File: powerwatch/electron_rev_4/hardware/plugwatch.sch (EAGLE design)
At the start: 127 parts, among them J1 CON_MICRO_SDDM3AT-SF-PEJM5, U1 BGA725L6-ALT, U10 SIP32510, U12 SIP32510, U13 AB1815-T3, U16 MAX6746, U2 SAFFB1G56KB0F0A, U20 DS2401P+, U3 IRM-03-5V, U4 MAX-M8, U5 OPA369, U6 LIS2DW12, U8 OPA369, U9 SIP32510, X1 ABS07-32.768KHZ-7-T

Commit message: renumbered eagle parts
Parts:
- removed C19: 0.1uF, passives:CAPACITOR0402_CAP
- removed C26: 4.7uF, passives:CAPACITOR0402_CAP
- removed D11: (no value), passives:DIODE_SCHOTTKYSOD323
- removed J4: (no value), SparkFun-Connectors:JST_2MM_MALE
- removed RF, RF1: 4.99k 1%, passives:RESISTOR0402_RES
- removed RI1, RI3: 953k 1%, passives:RESISTOR1206_RES_HIGH_CLEARANCE
- removed RI2, RI4: 953k 1%, passives:RESISTOR0402_RES
- removed U16: MAX6746, chips:MAX6746
- removed U20: DS2401P+, DS2401P+:DS2401P+
- added C10: 1uF, passives:CAPACITOR0402_CAP
- added C16: 100uF, passives:CAPACITOR1210_CAP
- added D2: (no value), passives:DIODE_SCHOTTKYSOD323
- added J2: (no value), SparkFun-Connectors:JST_2MM_MALE
- added R20: 34k, passives:RESISTOR0402_RES
- added R37, R38, R39, R40: 1M, passives:RESISTOR0402_RES
- added U11: SIP32510, chips:SIP32510
- added U14: (no value), microphones:SPH0645LM4H-B
- added V1: S14K385, varistor:S14K385
- C1: value 1uF -> 47pF
- C11: value 10nF -> 1uF
- C12: value 10nF -> 4.7uF; DESCRIPTION CAP CER 10000PF 50V X7R 0402 -> CAP CER 4.7UF 6.3V X5R 0402; DIGIKEY 490-7763-1-ND -> 445-5947-1-ND; MANUFACTURER Murata -> TDK; MPN GRM155R71H103JA88D -> C1005X5R0J475K050BC
- C15: value 100nF -> 100uF; device passives:CAPACITOR0402_CAP -> passives:CAPACITOR1210_CAP; DESCRIPTION CAP CER 0.1UF 10V X7R 0402 -> (none); DIGIKEY 490-10777-1-ND -> (none); MANUFACTURER Murata -> (none); MPN GRM155R71A104JA01D -> (none)
- C17: value 100uF -> 2000uF; device passives:CAPACITOR1210_CAP -> rcl:CPOL-USE5-13
- C2: value 2000uF -> 10nF; device rcl:CPOL-USE5-13 -> passives:CAPACITOR0402_CAP; DESCRIPTION (none) -> CAP CER 10000PF 50V X7R 0402; DIGIKEY (none) -> 490-7763-1-ND; MANUFACTURER (none) -> Murata; MPN (none) -> GRM155R71H103JA88D
- C3: value 47pF -> 10nF; DESCRIPTION (none) -> CAP CER 10000PF 50V X7R 0402; DIGIKEY (none) -> 490-7763-1-ND; MANUFACTURER (none) -> Murata; MPN (none) -> GRM155R71H103JA88D
- C4: value 1uF -> 0.1uF; DESCRIPTION CAP CER 10000PF 50V X7R 0402 -> CAP CER 0.1UF 10V X7R 0402; DIGIKEY 490-7763-1-ND -> 490-10777-1-ND; MPN GRM155R71H103JA88D -> GRM155R71A104JA01D
- C7: value 100uF -> 100nF; device passives:CAPACITOR1210_CAP -> passives:CAPACITOR0402_CAP; DESCRIPTION (none) -> CAP CER 0.1UF 10V X7R 0402; DIGIKEY (none) -> 490-10777-1-ND; MANUFACTURER (none) -> Murata; MPN (none) -> GRM155R71A104JA01D
- D1: value BLUE -> (none); device leds:LED0603 -> passives:DIODE_SCHOTTKYSOD323; DIGIKEY 160-1837-6-ND -> CUS10S30H3FCT-ND; MANUFACTURER (none) -> toshiba; MPN (none) -> CUS10S30,H3F
- D4: value 3.3V -> (none); device passives:DIODE_ZENERSOT323 -> passives:DIODE_SCHOTTKYSOD323; DIGIKEY MM3Z3V3BCT-ND -> CUS10S30H3FCT-ND; MANUFACTURER ON Semiconductor -> toshiba; MPN MM3Z3V3B -> CUS10S30,H3F
- D5, D6, D7: value 3.3V -> (none)
- D8: device passives:DIODE_SCHOTTKYSOD323 -> passives:DIODE_ZENERSOT323; DIGIKEY CUS10S30H3FCT-ND -> MM3Z3V3BCT-ND; MANUFACTURER toshiba -> ON Semiconductor; MPN CUS10S30,H3F -> MM3Z3V3B
- D9: value (none) -> BLUE; device passives:DIODE_SCHOTTKYSOD323 -> leds:LED0603; DIGIKEY CUS10S30H3FCT-ND -> 160-1837-6-ND; MANUFACTURER toshiba -> (none); MPN CUS10S30,H3F -> (none)
- R1: value 10k -> 66.5; DESCRIPTION RES SMD 150 OHM 1% 1/16W 0402 -> RES SMD 1K OHM 1% 1/16W 0402; DIGIKEY RMCF0402FT150RCT-ND -> RMCF0402FT1K00CT-ND; MPN RMCF0402FT150R -> RMCF0402FT1K00
- R10: value 10k -> 5k; DESCRIPTION RES SMD 10K OHM 1% 1/16W 0402 -> RES SMD 150 OHM 1% 1/16W 0402; DIGIKEY RMCF0402FT10K0CT-ND -> RMCF0402FT150RCT-ND; MPN RMCF0402FT10K0 -> RMCF0402FT150R
- R11: value 68 -> 10k
- R15: value 100k -> 10k; DESCRIPTION RES SMD 150 OHM 1% 1/16W 0402 -> RES SMD 10K OHM 1% 1/16W 0402; DIGIKEY RMCF0402FT150RCT-ND -> RMCF0402FT10K0CT-ND; MPN RMCF0402FT150R -> RMCF0402FT10K0
- R16, R17, R18, R19: value 100k -> 10k; DESCRIPTION RES SMD 100K OHM 1% 1/16W 0402 -> RES SMD 150 OHM 1% 1/16W 0402; DIGIKEY 1276-3432-1-ND -> RMCF0402FT150RCT-ND; MANUFACTURER Samsung -> Stackpole Electronics; MPN RC1005F104CS -> RMCF0402FT150R
- R2: value 10k -> 68; DESCRIPTION RES SMD 150 OHM 1% 1/16W 0402 -> RES SMD 10K OHM 1% 1/16W 0402; DIGIKEY RMCF0402FT150RCT-ND -> RMCF0402FT10K0CT-ND; MPN RMCF0402FT150R -> RMCF0402FT10K0
- R21: value 750k -> 100k; device passives:RESISTOR1206_RES_HIGH_CLEARANCE -> passives:RESISTOR0402_RES; DESCRIPTION RES SMD 150 OHM 1% 1/16W 0402 -> RES SMD 100K OHM 1% 1/16W 0402; DIGIKEY RMCF0402FT150RCT-ND -> 1276-3432-1-ND; MANUFACTURER Stackpole Electronics -> Samsung; MPN RMCF0402FT150R -> RC1005F104CS
- R22, R23: value 1M 1% -> 100k; DESCRIPTION (none) -> RES SMD 100K OHM 1% 1/16W 0402; DIGIKEY P1.00MLCT-ND -> 1276-3432-1-ND; MANUFACTURER (none) -> Samsung; MPN (none) -> RC1005F104CS
- R24: value 835k -> 100k; DESCRIPTION RES SMD 150 OHM 1% 1/16W 0402 -> RES SMD 100K OHM 1% 1/16W 0402; DIGIKEY RMCF0402FT150RCT-ND -> 1276-3432-1-ND; MANUFACTURER Stackpole Electronics -> Samsung; MPN RMCF0402FT150R -> RC1005F104CS
- R25: value 1M 1% -> 100k; DESCRIPTION (none) -> RES SMD 150 OHM 1% 1/16W 0402; DIGIKEY P1.00MLCT-ND -> RMCF0402FT150RCT-ND; MANUFACTURER (none) -> Stackpole Electronics; MPN (none) -> RMCF0402FT150R
- R26: value 68 -> 100k; DESCRIPTION RES SMD 10K OHM 1% 1/16W 0402 -> RES SMD 150 OHM 1% 1/16W 0402; DIGIKEY RMCF0402FT10K0CT-ND -> RMCF0402FT150RCT-ND; MPN RMCF0402FT10K0 -> RMCF0402FT150R
- R28: value 1M 1% -> 750k; device passives:RESISTOR0402_RES -> passives:RESISTOR1206_RES_HIGH_CLEARANCE; DESCRIPTION (none) -> RES SMD 150 OHM 1% 1/16W 0402; DIGIKEY P1.00MLCT-ND -> RMCF0402FT150RCT-ND; MANUFACTURER (none) -> Stackpole Electronics; MPN (none) -> RMCF0402FT150R
- R29: value 5K -> 750k; device passives:RESISTOR0402_RES -> passives:RESISTOR1206_RES_HIGH_CLEARANCE
- R32: value 1.5k -> 835k
- R33: value 1.5k -> 953k; DESCRIPTION RES SMD 150 OHM 1% 1/16W 0402 -> (none); DIGIKEY RMCF0402FT150RCT-ND -> P953KLCT-ND; MANUFACTURER Stackpole Electronics -> (none); MPN RMCF0402FT150R -> (none)
- R34: value 10k -> 953k; DESCRIPTION RES SMD 150 OHM 1% 1/16W 0402 -> (none); DIGIKEY RMCF0402FT150RCT-ND -> P953KLCT-ND; MANUFACTURER Stackpole Electronics -> (none); MPN RMCF0402FT150R -> (none)
- R35: value 66.5 -> 953k; device passives:RESISTOR0402_RES -> passives:RESISTOR1206_RES_HIGH_CLEARANCE; DESCRIPTION RES SMD 1K OHM 1% 1/16W 0402 -> (none); DIGIKEY RMCF0402FT1K00CT-ND -> P953KLCT-ND; MANUFACTURER Stackpole Electronics -> (none); MPN RMCF0402FT1K00 -> (none)
- R36: value 34k -> 953k; device passives:RESISTOR0402_RES -> passives:RESISTOR1206_RES_HIGH_CLEARANCE; DESCRIPTION RES SMD 1K OHM 1% 1/16W 0402 -> (none); DIGIKEY RMCF0402FT1K00CT-ND -> P953KLCT-ND; MANUFACTURER Stackpole Electronics -> (none); MPN RMCF0402FT1K00 -> (none)
- R4: value 1k -> 68; DESCRIPTION RES SMD 1K OHM 1% 1/16W 0402 -> RES SMD 10K OHM 1% 1/16W 0402; DIGIKEY RMCF0402FT1K00CT-ND -> RMCF0402FT10K0CT-ND; MPN RMCF0402FT1K00 -> RMCF0402FT10K0
- R5: value 100k -> 1k; DESCRIPTION RES SMD 150 OHM 1% 1/16W 0402 -> RES SMD 1K OHM 1% 1/16W 0402; DIGIKEY RMCF0402FT150RCT-ND -> RMCF0402FT1K00CT-ND; MPN RMCF0402FT150R -> RMCF0402FT1K00
- R6: value 10k -> 1.5k
- R7: value S14K385 -> 1.5k; device varistor:S14K385 -> passives:RESISTOR0402_RES; DESCRIPTION (none) -> RES SMD 150 OHM 1% 1/16W 0402; DIGIKEY (none) -> RMCF0402FT150RCT-ND; MANUFACTURER (none) -> Stackpole Electronics; MPN (none) -> RMCF0402FT150R
- R8: value 750k -> 4.99k; device passives:RESISTOR1206_RES_HIGH_CLEARANCE -> passives:RESISTOR0402_RES; DESCRIPTION RES SMD 150 OHM 1% 1/16W 0402 -> (none); DIGIKEY RMCF0402FT150RCT-ND -> P4.99KLCT-ND; MANUFACTURER Stackpole Electronics -> (none); MPN RMCF0402FT150R -> (none)
- R9: value 10k -> 4.99k; DESCRIPTION RES SMD 10K OHM 1% 1/16W 0402 -> (none); DIGIKEY RMCF0402FT10K0CT-ND -> P4.99KLCT-ND; MANUFACTURER Stackpole Electronics -> (none); MPN RMCF0402FT10K0 -> (none)
- U1: value BGA725L6-ALT -> AB1815-T3; device Particle:BGA725L6-ALT -> chips:AB1815-T3; DESCRIPTION IC AMP MMIC RF LNA 20DB TSLP-6 -> (none); DIGIKEY BGA725L6E6327FTSA1CT-ND -> (none); MANUFACTURER Infineon -> (none); MPN BGA725L6E6327FTSA1 -> (none)
- U10, U9: value SIP32510 -> OPA369; device chips:SIP32510 -> powerfilm:OPA369; DIGIKEY (none) -> 296-25252-1-ND
- U13: value AB1815-T3 -> SIP32510; device chips:AB1815-T3 -> chips:SIP32510
- U2: value SAFFB1G56KB0F0A -> BGA725L6-ALT; device Particle:FILTERS -> Particle:BGA725L6-ALT; ABACUS_TECHNOLOGIES SAFFB1G56KB0F0A -> (none); DESCRIPTION (none) -> IC AMP MMIC RF LNA 20DB TSLP-6; DIGIKEY (none) -> BGA725L6E6327FTSA1CT-ND; MANUFACTURER (none) -> Infineon; MPN (none) -> BGA725L6E6327FTSA1
- U3: value IRM-03-5V -> DS2401P+; device powerwatch:IRM-03-5V -> DS2401P+:DS2401P+; SPICEPREFIX (none) -> X
- U4: value MAX-M8 -> SAFFB1G56KB0F0A; device u-blox:MAX-M8 -> Particle:FILTERS; ABACUS_TECHNOLOGIES (none) -> SAFFB1G56KB0F0A; DESCRIPTION IC RECEIVER GPS/GNSS 18LCC -> (none); DIGIKEY 672-1003-1-ND -> (none); MANUFACTURER u-blox -> (none); MPN MAX-M8Q-0 -> (none)
- U5: value OPA369 -> IRM-03-5V; device powerfilm:OPA369 -> powerwatch:IRM-03-5V; DIGIKEY 296-25252-1-ND -> (none)
- U7: value (none) -> MAX-M8; device microphones:SPH0645LM4H-B -> u-blox:MAX-M8; DESCRIPTION (none) -> IC RECEIVER GPS/GNSS 18LCC; DIGIKEY (none) -> 672-1003-1-ND; MANUFACTURER (none) -> u-blox; MPN (none) -> MAX-M8Q-0
- U8: value OPA369 -> MAX6746; device powerfilm:OPA369 -> chips:MAX6746; DIGIKEY 296-25252-1-ND -> MAX6749KA
- renumbered A2 to A1, B2 to B1, C100 to C5, C101 to C6, C24 to C9, C27 to C14, C29 to C8, D10 to D3, L4 to L2, L5 to L3
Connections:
- net !EXTERNAL_RST: now also R19.2, TP26.TESTPOINT, U8.!RESET; no longer R1.2, TP17.TESTPOINT, U16.!RESET
- net !GPS_RESET: now also TP10.TESTPOINT, U7.!RESET; no longer TP23.TESTPOINT, U4.!RESET
- net !RTC_CS: now also R18.2, TP23.TESTPOINT, U1.!CS; no longer R6.2, TP11.TESTPOINT, U13.!CS
- net !RTC_INT1: now also R17.2, TP24.TESTPOINT, U1.FOUT/!IRQ1; no longer R34.2, TP15.TESTPOINT, U13.FOUT/!IRQ1
- net !SD_CS: now also TP18.TESTPOINT; no longer TP6.TESTPOINT
- net !SD_DETECT: now also R21.1, TP11.TESTPOINT; no longer R16.1, TP24.TESTPOINT
- net 5V: now also C15.1, C16.1, C17.+, R20.1, R25.1, U5.V+; no longer C17.1, C2.+, C7.1, R36.1, R5.1, U3.V+
- net AC/L-FUSED: now also R28.1, R35.1, U5.AC/L, V1.1; no longer R7.1, R8.1, RI1.1, U3.AC/L
- net AC/L-MEASURE: now also D1.CATHODE, D5.CATHODE; no longer D6.CATHODE, D8.CATHODE
- net AC/L-PERTURB: now also D2.CATHODE, D6.CATHODE, R28.2, TP27.TESTPOINT; no longer D4.CATHODE, D9.CATHODE, R8.2, TP25.TESTPOINT
- net AC/L-SENSE: now also R8.2, U9.OUT; no longer RF.2, U5.OUT
- net AC/N-FUSED: now also R29.1, R36.1, U5.AC/N, V1.2; no longer R21.1, R7.2, RI3.1, U3.AC/N
- net AC/N-MEASURE: now also D7.CATHODE, TP28.TESTPOINT; no longer D5.CATHODE, TP27.TESTPOINT
- net AC/N-PERTURB: now also D4.CATHODE, D8.CATHODE, R29.2; no longer D11.CATHODE, D7.CATHODE, R21.2
- net AC/N-SENSE: now also R9.2, U10.OUT; no longer RF1.2, U8.OUT
- net ACCEL_INT: now also TP8.TESTPOINT; no longer TP21.TESTPOINT
- net GND: now also C10.2, C11.2, C12.2, C15.2, C16.2, C17.-, C2.1, C3.1, C7.1, D1.ANODE, D2.ANODE, J2.-, R1.2, R16.2, R22.1, R24.1, R26.2, R33.1, R34.1, R38.1, R40.1, TP12.TESTPOINT, U1.!EXTR, U1.VSS, U10.VSS, U11.GND, U13.GND, U14.GND, U2.GND@1, U2.GND@4, U3.GND, U4.GND, U5.V-, U7.GND@1, U7.GND@10, U7.GND@12, U8.GND, U9.VSS; no longer C11.1, C12.1, C15.1, C17.2, C19.2, C2.-, C26.2, C3.2, C7.2, D11.ANODE, D9.ANODE, J4.-, R15.2, R17.1, R18.1, R19.1, R2.2, R28.1, R35.2, RI2.1, RI4.1, TP26.TESTPOINT, U1.GND@1, U1.GND@4, U10.GND, U13.!EXTR, U13.VSS, U16.GND, U2.GND, U20.GND, U3.V-, U4.GND@1, U4.GND@10, U4.GND@12, U5.VSS, U7.GND, U8.VSS, U9.GND
- net GPS_PWR_EN: now also R23.2, TP9.TESTPOINT, U11.EN; no longer R18.2, TP22.TESTPOINT, U10.EN
- net GPS_RF_IN: now also U4.OUTPUT, U7.RF_IN; no longer U2.OUTPUT, U4.RF_IN
- net GPS_RXD: now also TP6.TESTPOINT; no longer TP1.TESTPOINT
- net GPS_TXD: now also TP14.TESTPOINT; no longer TP2.TESTPOINT
- net GPS_VCC: now also C3.2, C7.2, R5.2, U11.VLOAD, U7.VCC, U7.VCC_IO, U7.V_BCKP; no longer C12.2, C15.2, R4.2, U10.VLOAD, U4.VCC, U4.VCC_IO, U4.V_BCKP
- net LNA_IN: now also U2.AI; no longer U1.AI
- net LNA_OUT: now also U2.AO, U4.INPUT; no longer U1.AO, U2.INPUT
- net MIC_BCLK: now also R3.2, TP22.TESTPOINT; no longer R11.2, TP10.TESTPOINT
- net MIC_DATA: now also R4.1, TP21.TESTPOINT; no longer R26.1, TP9.TESTPOINT
- net MIC_WS: now also R2.2, TP20.TESTPOINT; no longer R3.2, TP8.TESTPOINT
- net N$1: now also D9.ANODE, R5.1; no longer D1.ANODE, R4.1
- net N$10: now also R1.1, R20.2; no longer R35.1, R36.2
- net N$12: now also R3.1, U14.BCLK; no longer R11.1, U7.BCLK
- net N$13: now also C1.1, U1.AF; no longer C3.1, U13.AF
- net N$14: now also U13.VLOAD; no longer U9.VLOAD
- net N$15: now also R4.2, U14.DATA; no longer R26.2, U7.DATA
- net N$18: now also C12.1, R21.2; no longer C26.1, R16.2
- net N$2: now also D9.CATHODE, U7.TIMEPULSE; no longer D1.CATHODE, U4.TIMEPULSE
- net N$20: now also U1.XO; no longer U13.XO
- net N$21: now also U1.XI; no longer U13.XI
- net N$23: now also J2.+, R19.1, R32.1, U8.VCC, U8.WDS; no longer J4.+, R1.1, R24.1, U16.VCC, U16.WDS
- net N$25: now also R25.2, R26.1, U1.EXTI; no longer R15.1, R5.2, U13.EXTI
- net N$3: now also R2.1, U14.WS; no longer R3.1, U7.WS
- net N$31: now also R32.2, U8.!MR; no longer R24.2, U16.!MR
- net N$36: now also U8.SRT; no longer U16.SRT
- net N$39: now also U8.SWT; no longer U16.SWT
- net N$4: now also R6.2, R7.1; no longer R32.2, R33.1
- net N$40: now also U7.TXD; no longer U4.TXD
- net N$41: now also U7.RXD; no longer U4.RXD
- net N$42: now also R37.1, R38.2, U9.IN+; no longer R22.1, R23.2, U5.IN+
- net N$43: now also R33.2, R35.2, R8.1, U9.IN-; no longer RF.1, RI1.2, RI2.2, U5.IN-
- net N$44: now also R39.1, R40.2, U10.IN+; no longer R25.1, R28.2, U8.IN+
- net N$45: now also R34.2, R36.2, R9.1, U10.IN-; no longer RF1.1, RI3.2, RI4.2, U8.IN-
- net N$5: now also R7.2, U1.VBAT; no longer R33.2, U13.VBAT
- net SD_ENABLE: now also R22.2, TP19.TESTPOINT; no longer R17.2, TP7.TESTPOINT
- net SD_MISO: now also TP16.TESTPOINT, U1.SDO; no longer TP4.TESTPOINT, U13.SDO
- net SD_MOSI: now also TP15.TESTPOINT, U1.SDI; no longer TP3.TESTPOINT, U13.SDI
- net SD_SCLK: now also TP17.TESTPOINT, U1.SCL; no longer TP5.TESTPOINT, U13.SCL
- net SENSORS_SCL: now also R15.1, TP7.TESTPOINT; no longer R9.1, TP20.TESTPOINT
- net SENSORS_SDA: now also R11.1, TP5.TESTPOINT; no longer R10.1, TP19.TESTPOINT
- net SERIAL_NUM: now also R10.2, TP13.TESTPOINT, U3.DATA; no longer R29.2, TP28.TESTPOINT, U20.DATA
- net VCC: now also C10.1, C11.1, R10.1, R11.2, R15.2, R17.1, R18.1, R37.2, R39.2, TP4.TESTPOINT, U1.VCC, U10.VCC, U11.VSUPP, U13.VSUPP, U14.SELECT, U14.VDD, U9.VCC; no longer C1.1, C19.1, R10.2, R22.2, R25.2, R29.1, R32.1, R34.1, R9.2, TP18.TESTPOINT, U10.VSUPP, U13.VCC, U5.VCC, U7.SELECT, U7.VDD, U8.VCC, U9.VSUPP
- net VCC_RF: now also C2.2, U2.PON, U2.VCC, U7.VCC_RF; no longer C11.2, U1.PON, U1.VCC, U4.VCC_RF
- net WDI: now also R16.1, TP25.TESTPOINT, U1.WDI, U8.WDI; no longer R2.1, TP16.TESTPOINT, U13.WDI, U16.WDI
- net WIFI_PWR_EN: now also R24.2, TP1.TESTPOINT, U13.EN; no longer R19.2, TP12.TESTPOINT, U9.EN
- net WIFI_RXD: now also TP3.TESTPOINT; no longer TP14.TESTPOINT
- net WIFI_TXD: now also TP2.TESTPOINT; no longer TP13.TESTPOINT
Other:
- note added: "3.3V Zener Diode"

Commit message: start adding part numbers and such
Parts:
- D5, D6: DIGIKEY MM3Z3V3BCT-ND -> RMCF0402FT1M00CT-ND
- R28, R29, R30, R31: DESCRIPTION RES SMD 150 OHM 1% 1/16W 0402 -> (none); DIGIKEY RMCF0402FT150RCT-ND -> 311-750KFRCT-ND; MANUFACTURER Stackpole Electronics -> Yageo; MPN RMCF0402FT150R -> RC1206FR-07750KL
- R33, R34: DIGIKEY P953KLCT-ND -> YAG3262CT-ND; MANUFACTURER (none) -> Yageo; MPN (none) -> RC0402FR-07953KL
- R35, R36: DIGIKEY P953KLCT-ND -> P953KBCCT-ND; MANUFACTURER (none) -> Panasonic Electronic Components; MPN (none) -> ERA-8AEB9533V
- R37, R38, R39, R40: DIGIKEY P1.00MLCT-ND -> RMCF0402FT1M00CT-ND; MANUFACTURER (none) -> Stackpole Electronics Inc.; MPN (none) -> RMCF0402FT1M00
- R8, R9: MANUFACTURER (none) -> Panasonic Electronic Components; MPN (none) -> ERJ-2RKF4991X

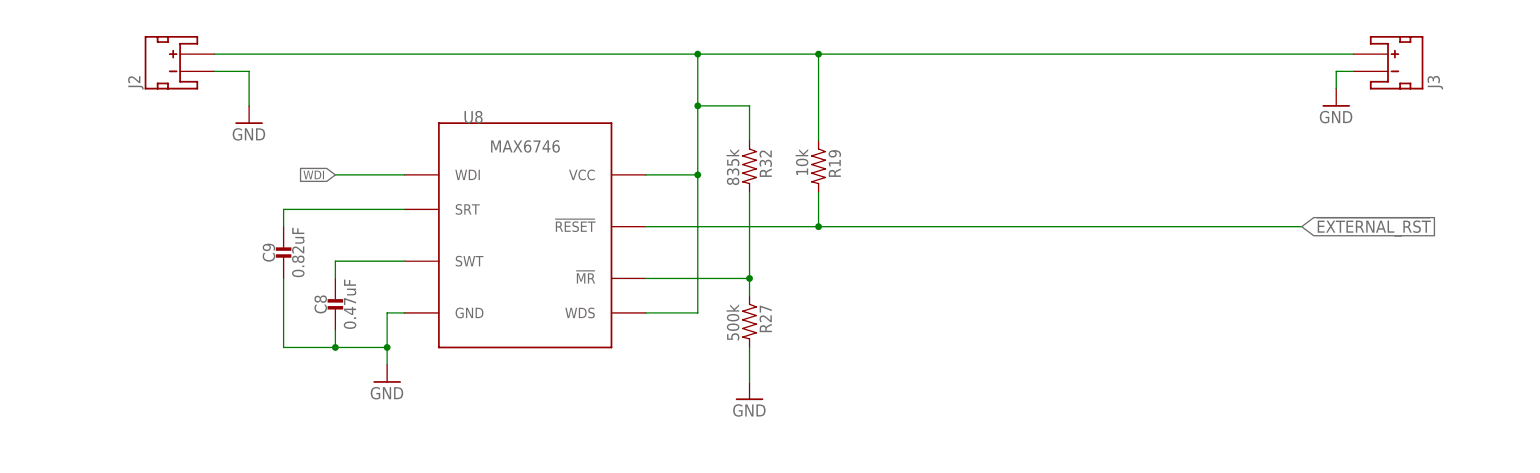
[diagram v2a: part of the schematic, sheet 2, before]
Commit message: fixed up BOM and attributes
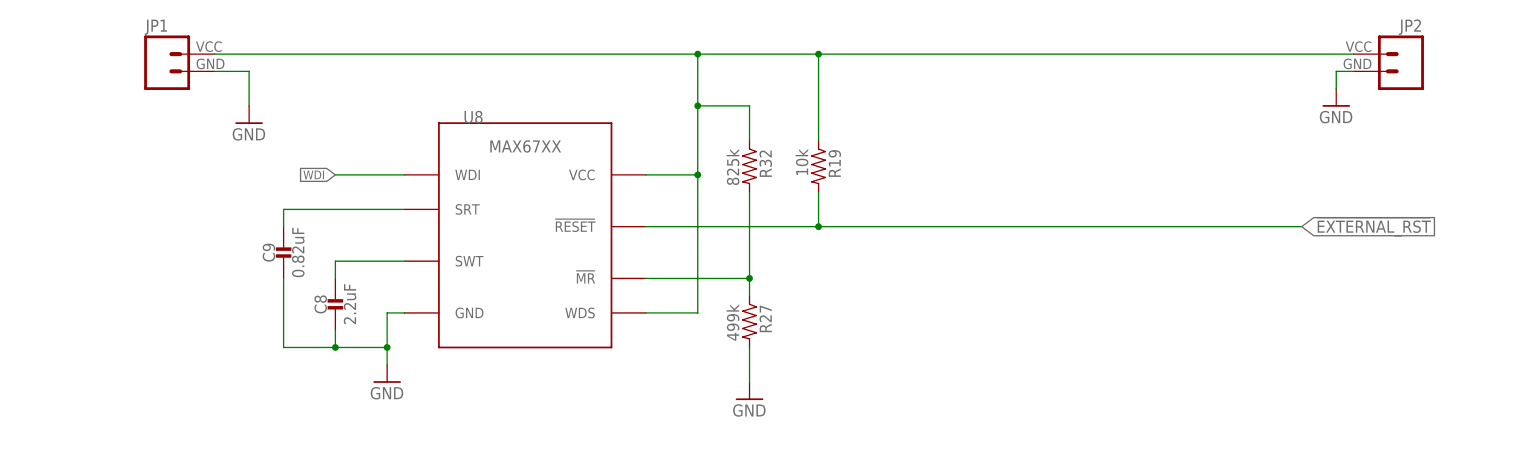
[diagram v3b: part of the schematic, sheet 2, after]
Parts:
- removed J2, J3: (no value), SparkFun-Connectors:JST_2MM_MALE
- added JP1, JP2: (no value), SparkFun-Connectors:M024UCON-15767
- C1: DESCRIPTION (none) -> CAP CER 47PF 100V C0G/NP0 0402; DIGIKEY (none) -> 490-7307-1-ND; MANUFACTURER (none) -> Murata Electronics North America; MPN (none) -> GRM1555C2A470JA01D
- C10: DESCRIPTION (none) -> CAP CER 1UF 10V X7S 0402; DIGIKEY (none) -> 490-13409-1-ND; MANUFACTURER (none) -> Murata Electronics North America; MPN (none) -> GCM155C71A105KE38D
- C11: DESCRIPTION CAP CER 10000PF 50V X7R 0402 -> CAP CER 1UF 10V X7S 0402; DIGIKEY 490-7763-1-ND -> 490-13409-1-ND; MANUFACTURER Murata -> Murata Electronics North America; MPN GRM155R71H103JA88D -> GCM155C71A105KE38D
- C13: DESCRIPTION CAP CER 10000PF 50V X7R 0402 -> CAP CER 10UF 6.3V X5R 0402; DIGIKEY 490-7763-1-ND -> 490-13211-1-ND; MANUFACTURER Murata -> Murata Electronics North America; MPN GRM155R71H103JA88D -> GRJ155R60J106ME11D
- C14: device passives:CAPACITOR0805_CAP -> passives:CAPACITOR0402_CAP; DESCRIPTION CAP CER 10UF 10V X7R 0805 -> CAP CER 10UF 6.3V X5R 0402; DIGIKEY 490-8316-1-ND -> 490-13211-1-ND; MANUFACTURER Murata -> Murata Electronics North America; MPN GRM21BR71A106ME51L -> GRJ155R60J106ME11D
- C15, C16: DESCRIPTION (none) -> CAP CER 100UF 6.3V X7S 1210; DIGIKEY (none) -> 490-10530-1-ND; MANUFACTURER (none) -> Murata Electronics North America; MPN (none) -> GRM32EC70J107ME15L
- C17: DESCRIPTION (none) -> CAP ALUM 2000UF 20% 6.3V T/H; DIGIKEY (none) -> P122284TB-ND; MANUFACTURER (none) -> Panasonic Electronic Components; MPN (none) -> EEU-FS0J202B
- C2, C3: DESCRIPTION CAP CER 10000PF 50V X7R 0402 -> CAP CER 10000PF 16V X7R 0402; DIGIKEY 490-7763-1-ND -> 490-1313-1-ND; MANUFACTURER Murata -> Murata Electronics North America; MPN GRM155R71H103JA88D -> GRM155R71C103KA01D
- C4: DESCRIPTION CAP CER 0.1UF 10V X7R 0402 -> CAP CER 0.1UF 10V X5R 0402; DIGIKEY 490-10777-1-ND -> 311-1336-1-ND; MANUFACTURER Murata -> Yageo; MPN GRM155R71A104JA01D -> CC0402KRX5R6BB104
- C5, C6: DESCRIPTION (none) -> CAP CER 0.1UF 10V X5R 0402; DIGIKEY (none) -> 311-1336-1-ND; MANUFACTURER (none) -> Yageo; MPN (none) -> CC0402KRX5R6BB104
- C7: value 100nF -> 0.1uF; DESCRIPTION CAP CER 0.1UF 10V X7R 0402 -> CAP CER 0.1UF 10V X5R 0402; DIGIKEY 490-10777-1-ND -> 311-1336-1-ND; MANUFACTURER Murata -> Yageo; MPN GRM155R71A104JA01D -> CC0402KRX5R6BB104
- C8: value 0.47uF -> 2.2uF; DIGIKEY (none) -> 490-12696-1-ND; MANUFACTURER (none) -> Murata Electronics North America; MPN (none) -> GRM155C70J225KE11D
- C9: DIGIKEY (none) -> 490-10440-1-ND; MANUFACTURER (none) -> Murata Electronics North America; MPN (none) -> GRM155C80J824KE15D
- D5, D6: DESCRIPTION (none) -> DIODE ZENER 3.3V 200MW SOD323F; DIGIKEY RMCF0402FT1M00CT-ND -> MM3Z3V3BCT-ND; MANUFACTURER ON Semiconductor -> ON Semiconductor; MPN MM3Z3V3B -> MM3Z3V3B
- D7, D8: DESCRIPTION (none) -> DIODE ZENER 3.3V 200MW SOD323F; DIGIKEY MM3Z3V3BCT-ND -> MM3Z3V3BCT-ND; MANUFACTURER ON Semiconductor -> ON Semiconductor; MPN MM3Z3V3B -> MM3Z3V3B
- D9: DESCRIPTION (none) -> LED BLUE CLEAR SMD; DIGIKEY 160-1837-6-ND -> 160-1837-6-ND; MANUFACTURER (none) -> Lite-On Inc.; MPN (none) -> LTST-C194TBKT
- F1: DESCRIPTION (none) -> FUSE BRD MNT 500MA 350VAC 100VDC
- J1: value CON_MICRO_SDDM3AT-SF-PEJM5 -> DM3AT-SF-PEJM5; device connector:CON_MICRO_SDDM3AT-SF-PEJM5 -> connector:DM3AT-SF-PEJM5
- R1: DESCRIPTION RES SMD 1K OHM 1% 1/16W 0402 -> RES SMD 66.5 OHM 1% 1/16W 0402; DIGIKEY RMCF0402FT1K00CT-ND -> YAG3210CT-ND; MANUFACTURER Stackpole Electronics -> Yageo; MPN RMCF0402FT1K00 -> RC0402FR-0766R5L
- R10: value 5k -> 5.1k; DESCRIPTION RES SMD 150 OHM 1% 1/16W 0402 -> RES SMD 5.1K OHM 1% 1/10W 0402; DIGIKEY RMCF0402FT150RCT-ND -> P5.10KLCT-ND; MANUFACTURER Stackpole Electronics -> Panasonic Electronic Components; MPN RMCF0402FT150R -> ERJ-2RKF5101X
- R11, R12, R13, R14, R15: DESCRIPTION RES SMD 10K OHM 1% 1/16W 0402 -> RES SMD 10K OHM 1% 1/16W 0402; DIGIKEY RMCF0402FT10K0CT-ND -> RMCF0402FT10K0CT-ND; MANUFACTURER Stackpole Electronics -> Stackpole Electronics Inc.; MPN RMCF0402FT10K0 -> RMCF0402FT10K0
- R16, R17, R18, R19: DESCRIPTION RES SMD 150 OHM 1% 1/16W 0402 -> RES SMD 10K OHM 1% 1/16W 0402; DIGIKEY RMCF0402FT150RCT-ND -> RMCF0402FT10K0CT-ND; MANUFACTURER Stackpole Electronics -> Stackpole Electronics Inc.; MPN RMCF0402FT150R -> RMCF0402FT10K0
- R2, R3, R4: DESCRIPTION RES SMD 10K OHM 1% 1/16W 0402 -> RES SMD 68 OHM 1% 1/16W 0402; DIGIKEY RMCF0402FT10K0CT-ND -> 311-68.0LRCT-ND; MANUFACTURER Stackpole Electronics -> Yageo; MPN RMCF0402FT10K0 -> RC0402FR-0768RL
- R20: DESCRIPTION RES SMD 1K OHM 1% 1/16W 0402 -> RES SMD 34K OHM 1% 1/10W 0402; DIGIKEY RMCF0402FT1K00CT-ND -> P34.0KLCT-ND; MANUFACTURER Stackpole Electronics -> Panasonic Electronic Components; MPN RMCF0402FT1K00 -> ERJ-2RKF3402X
- R21, R22, R23, R24: DIGIKEY 1276-3432-1-ND -> 541-100KLCT-ND; MANUFACTURER Samsung -> Vishay Dale; MPN RC1005F104CS -> CRCW0402100KFKED
- R25, R26: DESCRIPTION RES SMD 150 OHM 1% 1/16W 0402 -> RES SMD 100K OHM 1% 1/16W 0402; DIGIKEY RMCF0402FT150RCT-ND -> 541-100KLCT-ND; MANUFACTURER Stackpole Electronics -> Vishay Dale; MPN RMCF0402FT150R -> CRCW0402100KFKED
- R27: value 500k -> 499k; DESCRIPTION RES SMD 150 OHM 1% 1/16W 0402 -> RES SMD 499K OHM 1% 1/10W 0402; DIGIKEY RMCF0402FT150RCT-ND -> P499KLCT-ND; MANUFACTURER Stackpole Electronics -> Panasonic Electronic Components; MPN RMCF0402FT150R -> ERJ-2RKF4993X
- R28, R29, R30, R31: DESCRIPTION (none) -> RES SMD 750K OHM 1% 1/4W 1206
- R32: value 835k -> 825k; DESCRIPTION RES SMD 150 OHM 1% 1/16W 0402 -> RES SMD 825K OHM 1% 1/10W 0402; DIGIKEY RMCF0402FT150RCT-ND -> P825KLCT-ND; MANUFACTURER Stackpole Electronics -> Panasonic Electronic Components; MPN RMCF0402FT150R -> ERJ-2RKF8253X
- R33, R34: DESCRIPTION (none) -> RES SMD 953K OHM 1% 1/16W 0402
- R37, R38, R39, R40: DESCRIPTION (none) -> RES 1M OHM 1% 1/16W 0402
- R6, R7: DESCRIPTION RES SMD 150 OHM 1% 1/16W 0402 -> RES SMD 1.5K OHM 0.1% 1/16W 0402; DIGIKEY RMCF0402FT150RCT-ND -> P1.5KDCCT-ND; MANUFACTURER Stackpole Electronics -> Panasonic Electronic Components; MPN RMCF0402FT150R -> ERA-2AEB152X
- R8, R9: DESCRIPTION (none) -> RES SMD 4.99K OHM 1% 1/10W 0402
- U4: ABACUS_TECHNOLOGIES SAFFB1G56KB0F0A -> (none); DESCRIPTION (none) -> FILTER SAW 1.582GHZ 5SMD; DIGIKEY (none) -> 587-3990-1-ND; MANUFACTURER (none) -> Taiyo Yuden; MPN (none) -> F6QA1G582H2JM-J
- U8: value MAX6746 -> MAX67XXMAX6749MAX67XX; device chips:MAX6746 -> chips:MAX67XXMAX6749MAX67XX
- V1: DESCRIPTION (none) -> VARISTOR 620V 5KA DISC 14MM; DIGIKEY (none) -> 495-5945-ND; MANUFACTURER (none) -> EPCOS (TDK); MPN (none) -> B72214S2381K101
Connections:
- net GND: now also JP1.1, JP2.1; no longer J2.-, J3.-
- net N$23: now also JP1.2, JP2.2; no longer J2.+, J3.+
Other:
- note added: "Watchdog Timeout = 1137s Reset Period = ~4s"
- note removed: "Watchdog Timeout = 297s Reset Period = ~4s"
